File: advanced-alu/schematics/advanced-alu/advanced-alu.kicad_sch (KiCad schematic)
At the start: 2 parts

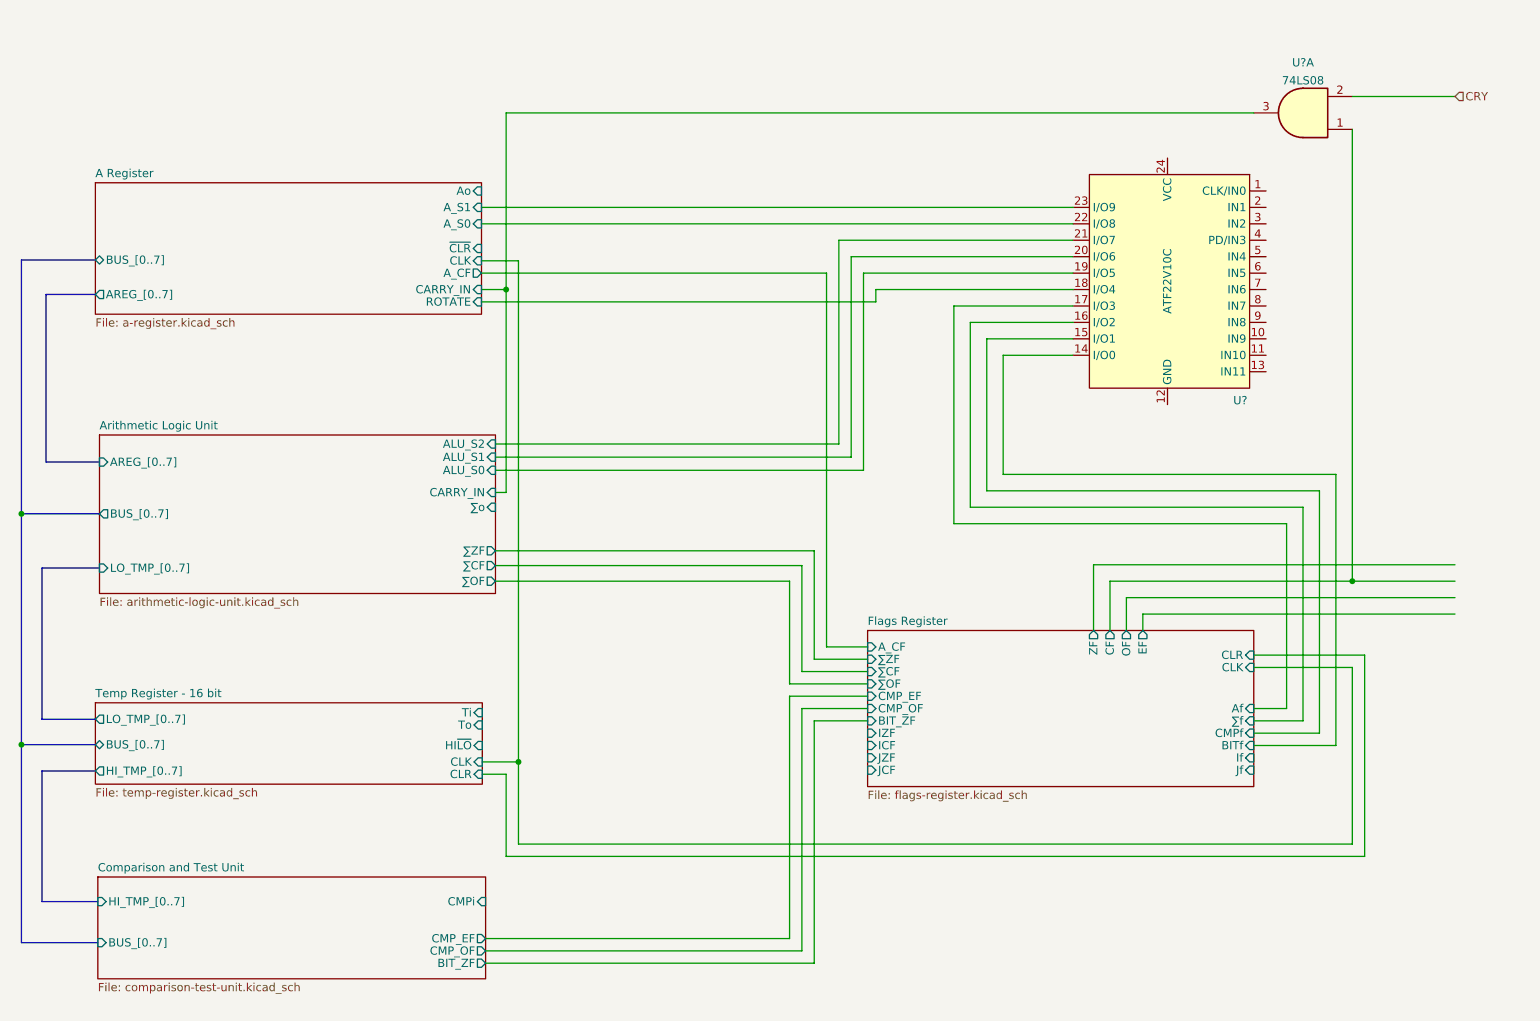
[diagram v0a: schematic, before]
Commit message: first complete draft for advanced ALU
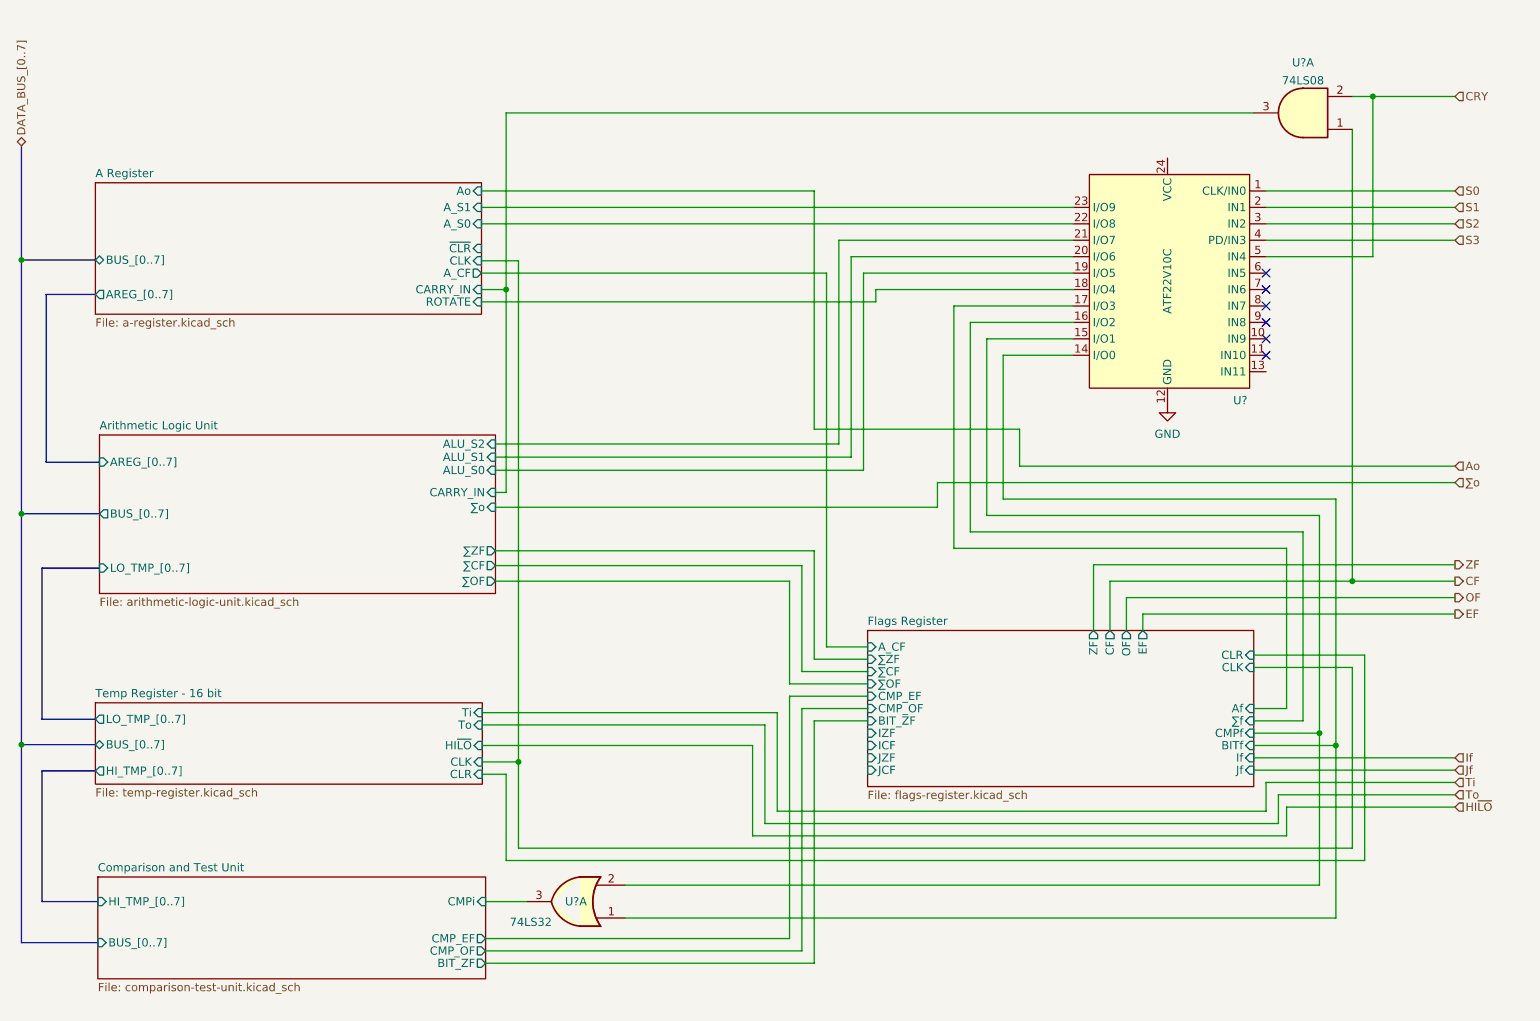
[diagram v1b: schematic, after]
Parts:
- added U?: 74LS32, symbol 74xx:74LS32
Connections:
- net CRY: now also U?.5 (IN4)
- net Comparison and Test Unit/CMPi: now also U?.3
- net Flags Register/BITf: now also U?.1
- net Flags Register/CMPf: now also U?.2
- net S0: now reaches U?.1 (CLK/IN0)
- net GND: now reaches U?.12 (GND)
- net S1: now reaches U?.2 (IN1)
- net S2: now reaches U?.3 (IN2)
- net S3: now reaches U?.4 (PD/IN3)
- net Flags Register/CF renamed CF
- no-connect marks 0 -> 6

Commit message: corrected issues
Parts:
- added U?: 74LS04, symbol 74xx:74LS04
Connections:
- net A Register/~{CLR}: now also U?.2
- net VCC: now reaches U?.24 (VCC)
- new net CLR: U?.1
- no-connect marks 6 -> 7
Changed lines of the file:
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@@
   (junction (at 259.715 22.86) (diameter 0) (color 0 0 0 0)
   )
+  (junction (at 256.54 139.065) (diameter 0) (color 0 0 0 0)
+  )
   (junction (at 50.8 48.133) (diameter 0) (color 0 0 0 0)
   )
@@
   (junction (at 50.8 87.376) (diameter 0) (color 0 0 0 0)
   )
+  (junction (at 125.73 127.635) (diameter 0) (color 0 0 0 0)
+  )
   (junction (at 251.46 121.285) (diameter 0) (color 0 0 0 0)
   )
@@
   (junction (at 254 123.19) (diameter 0) (color 0 0 0 0)
   )
+  (junction (at 258.445 140.97) (diameter 0) (color 0 0 0 0)
+  )
   (junction (at 50.8 123.063) (diameter 0) (color 0 0 0 0)
   )
+  (no_connect (at 243.205 65.405))
   (no_connect (at 243.205 52.705))
   (no_connect (at 243.205 55.245))
@@
     (stroke (width 0) (type default) (color 0 0 0 0))
   )
+  (wire (pts (xy 135.255 127.635) (xy 135.255 73.66))
+    (stroke (width 0) (type default) (color 0 0 0 0))
+  )
   (wire (pts (xy 173.355 156.845) (xy 173.355 119.38))
     (stroke (width 0) (type default) (color 0 0 0 0))
@@
     (stroke (width 0) (type default) (color 0 0 0 0))
   )
+  (wire (pts (xy 135.255 58.42) (xy 135.255 46.355))
+    (stroke (width 0) (type default) (color 0 0 0 0))
+  )
   (wire (pts (xy 245.11 130.81) (xy 272.415 130.81))
     (stroke (width 0) (type default) (color 0 0 0 0))
@@
     (stroke (width 0) (type default) (color 0 0 0 0))
   )
+  (wire (pts (xy 125.73 127.635) (xy 135.255 127.635))
+    (stroke (width 0) (type default) (color 0 0 0 0))
+  )
   (wire (pts (xy 248.92 90.17) (xy 248.92 119.38))
     (stroke (width 0) (type default) (color 0 0 0 0))
@@
     (stroke (width 0) (type default) (color 0 0 0 0))
   )
+  (wire (pts (xy 258.445 140.97) (xy 272.415 140.97))
+    (stroke (width 0) (type default) (color 0 0 0 0))
+  )
   (wire (pts (xy 254 123.19) (xy 254 149.86))
     (stroke (width 0) (type default) (color 0 0 0 0))
@@
     (stroke (width 0) (type default) (color 0 0 0 0))
   )
+  (wire (pts (xy 256.54 139.065) (xy 272.415 139.065))
+    (stroke (width 0) (type default) (color 0 0 0 0))
+  )
   (wire (pts (xy 122.047 123.19) (xy 163.83 123.19))
     (stroke (width 0) (type default) (color 0 0 0 0))
@@
     (stroke (width 0) (type default) (color 0 0 0 0))
   )
+  (wire (pts (xy 135.255 46.355) (xy 121.92 46.355))
+    (stroke (width 0) (type default) (color 0 0 0 0))
+  )
   (wire (pts (xy 197.485 90.17) (xy 248.92 90.17))
     (stroke (width 0) (type default) (color 0 0 0 0))
@@
     (effects (font (size 1.27 1.27)) (justify left))
   )
+  (hierarchical_label "CLK" (shape input) (at 272.415 139.065 0)
+    (effects (font (size 1.27 1.27)) (justify left))
+  )
   (hierarchical_label "CRY" (shape input) (at 272.415 22.86 0)
     (effects (font (size 1.27 1.27)) (justify left))
@@
   )
   (hierarchical_label "OF" (shape output) (at 272.415 100.33 0)
+    (effects (font (size 1.27 1.27)) (justify left))
+  )
+  (hierarchical_label "CLR" (shape input) (at 272.415 140.97 0)
     (effects (font (size 1.27 1.27)) (justify left))
   )
@@
     (pin "2")
     (pin "3")
+  )
+  (symbol (lib_id "74xx:74LS04") (at 135.255 66.04 90) (unit 1)
+    (in_bom yes) (on_board yes) (fields_autoplaced)
+    (property "Reference" "U?" (id 0) (at 139.827 65.1315 90)
+      (effects (font (size 1.27 1.27)) (justify right))
+    )
+    (property "Value" "74LS04" (id 1) (at 139.827 67.9066 90)
+      (effects (font (size 1.27 1.27)) (justify right))
+    )
+    (property "Footprint" "" (id 2) (at 135.255 66.04 0)
+      (effects (font (size 1.27 1.27)) hide)
+    )
+    (property "Datasheet" "http://www.ti.com/lit/gpn/sn74LS04" (id 3) (at 135.255 66.04 0)
+      (effects (font (size 1.27 1.27)) hide)
+    )
+    (pin "1")
+    (pin "2")
   )
   (symbol (lib_id "common-symbols:ATF22V10C") (at 227.965 51.435 0) (mirror y) (unit 1)
@@
     (pin "1")
   )
+  (symbol (lib_id "power:VCC") (at 227.965 32.385 0) (unit 1)
+    (in_bom yes) (on_board yes) (fields_autoplaced)
+    (property "Reference" "#PWR?" (id 0) (at 227.965 36.195 0)
+      (effects (font (size 1.27 1.27)) hide)
+    )
+    (property "Value" "VCC" (id 1) (at 227.965 28.7805 0))
+    (property "Footprint" "" (id 2) (at 227.965 32.385 0)
+      (effects (font (size 1.27 1.27)) hide)
+    )
+    (property "Datasheet" "" (id 3) (at 227.965 32.385 0)
+      (effects (font (size 1.27 1.27)) hide)
+    )
+    (pin "1")
+  )
   (symbol (lib_id "74xx:74LS08") (at 248.92 25.4 180) (unit 1)
     (in_bom yes) (on_board yes) (fields_autoplaced)
@@
       (reference "#PWR?") (unit 1) (value "VCC") (footprint "")
     )
+    (path "/b941cd8b-e40a-47fb-b73a-08c06ea6c665"
+      (reference "#PWR?") (unit 1) (value "VCC") (footprint "")
+    )
     (path "/81d36f22-4986-4730-8521-7cec07d7e235/c626e370-a5ce-47bd-b258-516265b4ca6f"
       (reference "#PWR?") (unit 1) (value "VCC") (footprint "")
@@
       (reference "U?") (unit 1) (value "74LS04") (footprint "")
     )
+    (path "/5863a2ec-a18a-49d1-98fe-a9e00abbf4b1"
+      (reference "U?") (unit 1) (value "74LS04") (footprint "")
+    )

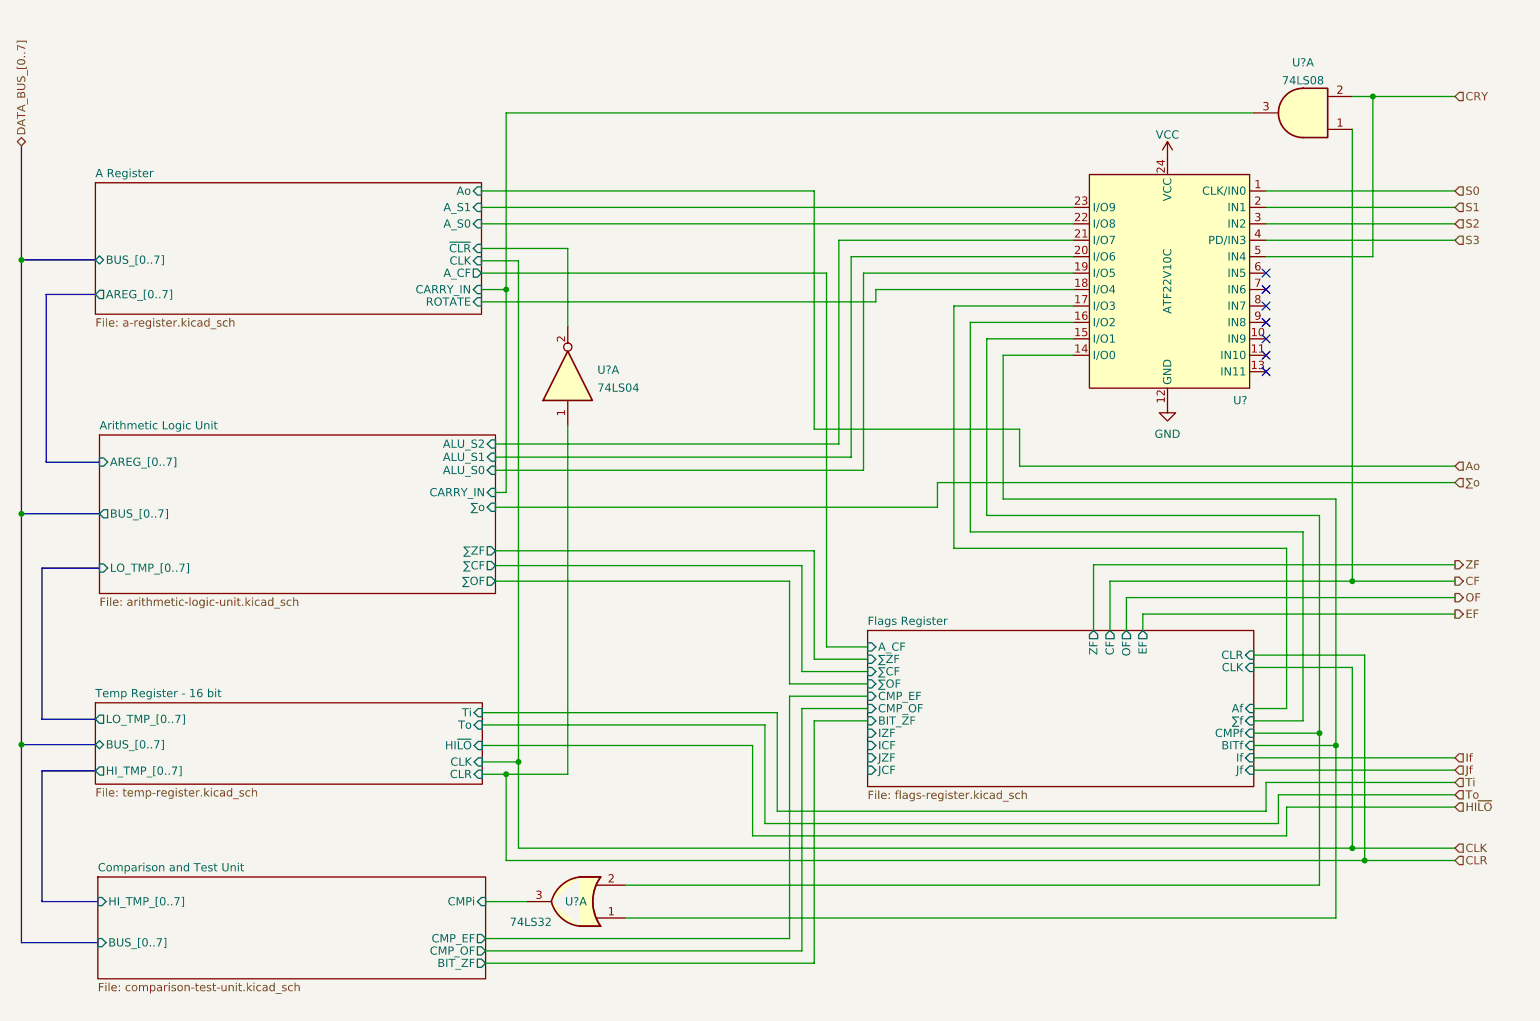
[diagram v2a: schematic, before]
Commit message: enabled a compare to zero operation
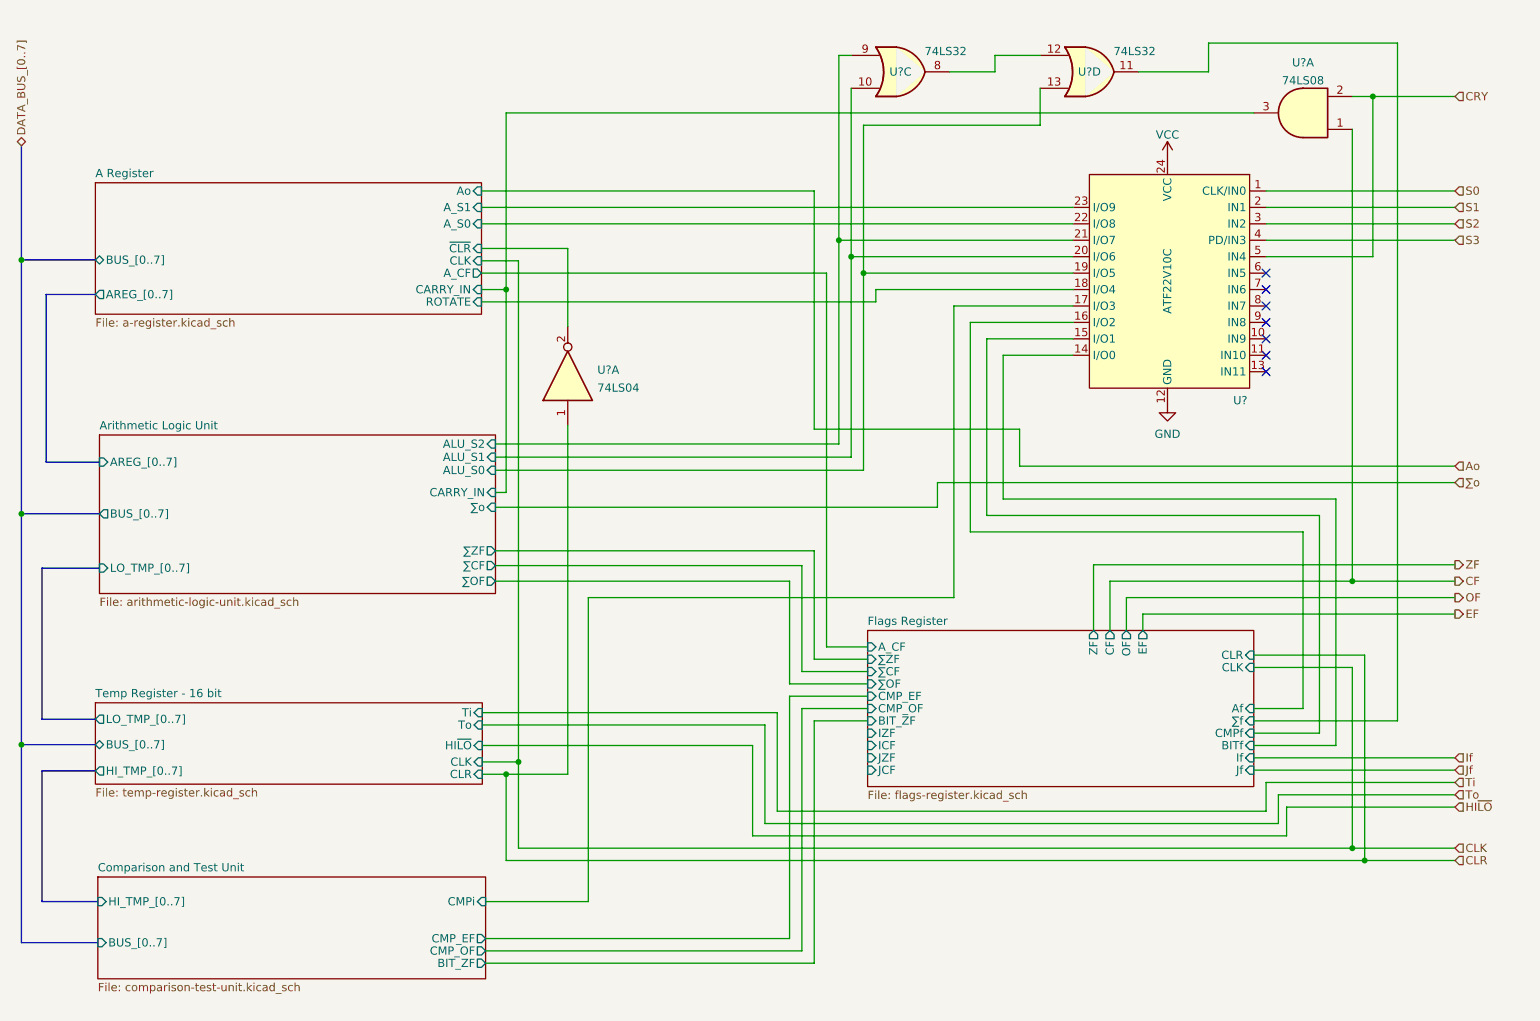
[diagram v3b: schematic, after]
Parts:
- removed U?: 74LS32, symbol 74xx:74LS32
- added U? (x2): 74LS32, symbol 74xx:74LS32
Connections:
- net Arithmetic Logic Unit/ALU_S0: now also U?.13
- net Arithmetic Logic Unit/ALU_S1: now also U?.10
- net Arithmetic Logic Unit/ALU_S2: now also U?.9
- net Comparison and Test Unit/CMPi: now also U?.17 (I/O3)
- net Flags Register/Af: now also U?.16 (I/O2); no longer U?.17 (I/O3)
- net Flags Register/∑f: now also U?.11; no longer U?.16 (I/O2)
- new net: U?.12, U?.8

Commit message: updated ALU design
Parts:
- removed U? (x2): 74LS32, symbol 74xx:74LS32
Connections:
- net Comparison and Test Unit/CMPi is gone; now on net Flags Register/Af: U?.17 (I/O3)
- net Flags Register/Af: no longer U?.16 (I/O2)
- net CMPi: now reaches U?.6 (IN5)
- new net Flags Register/ALUf: U?.16 (I/O2)
- no-connect marks 7 -> 6
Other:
- sheet Flags Register ports: added ALUf, BUS_[0..7], Fo; removed ∑f
